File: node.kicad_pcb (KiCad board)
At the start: 2 copper layers, 46 x 38 mm, 38 parts, among them J1 USB_B_Mini, J2 TC2030_NL, J3 FFC-0.5MM-6POS, J4 Port_1, J5 Port_2, J6 FFC-0.5MM-6POS, J7 Port_3, J8 Port_4, U1 PMIC-LDO-XC6204B332MR_SOT23-5_, U2 LP2985-5.0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

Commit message: Replace 2x1 header footprint by port footprint
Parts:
- J4, J5, J7, J8: footprint Connector_PinHeader_2.54mm:PinHeader_1x02_P2.54mm_Vertical -> node:port
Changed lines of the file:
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@@
       (net 15 "Net-(D4-Pad1)"))
   )
-  (module Connector_PinHeader_2.54mm:PinHeader_1x02_P2.54mm_Vertical (layer F.Cu)
+  (module node:port (layer F.Cu)
     (at 127.254 79.629 90)
     (descr "Through hole straight pin header, 1x02, 2.54mm pitch, single row")
     (tags "Through hole pin header THT 1x02 2.54mm single row")
-    (fp_text reference J4 (at 0 -2.33 90) (layer F.SilkS) hide
+    (fp_text reference J4 (at -0.254 -1.778 90) (layer F.SilkS) hide
       (effects (font (size 1 1) (thickness 0.15)))
     )
-    (fp_text value Port_1 (at 0 4.87 90) (layer F.Fab)
+    (fp_text value Port_1 (at 0 4.318 90) (layer F.Fab)
       (effects (font (size 1 1) (thickness 0.15)))
     )
-    (fp_text user %R (at 0 1.27 180) (layer F.Fab)
-      (effects (font (size 1 1) (thickness 0.15)))
-    )
-    (fp_line (start 1.8 -1.8) (end -1.8 -1.8) (layer F.CrtYd) (width 0.05))
-    (fp_line (start 1.8 4.35) (end 1.8 -1.8) (layer F.CrtYd) (width 0.05))
-    (fp_line (start -1.8 4.35) (end 1.8 4.35) (layer F.CrtYd) (width 0.05))
-    (fp_line (start -1.8 -1.8) (end -1.8 4.35) (layer F.CrtYd) (width 0.05))
-    (fp_line (start -1.33 -1.33) (end 0 -1.33) (layer F.SilkS) (width 0.12))
-    (fp_line (start -1.33 0) (end -1.33 -1.33) (layer F.SilkS) (width 0.12))
-    (fp_line (start -1.33 1.27) (end 1.33 1.27) (layer F.SilkS) (width 0.12))
-    (fp_line (start 1.33 1.27) (end 1.33 3.87) (layer F.SilkS) (width 0.12))
-    (fp_line (start -1.33 1.27) (end -1.33 3.87) (layer F.SilkS) (width 0.12))
-    (fp_line (start -1.33 3.87) (end 1.33 3.87) (layer F.SilkS) (width 0.12))
-    (fp_line (start -1.27 -0.635) (end -0.635 -1.27) (layer F.Fab) (width 0.1))
-    (fp_line (start -1.27 3.81) (end -1.27 -0.635) (layer F.Fab) (width 0.1))
-    (fp_line (start 1.27 3.81) (end -1.27 3.81) (layer F.Fab) (width 0.1))
-    (fp_line (start 1.27 -1.27) (end 1.27 3.81) (layer F.Fab) (width 0.1))
-    (fp_line (start -0.635 -1.27) (end 1.27 -1.27) (layer F.Fab) (width 0.1))
-    (pad 2 thru_hole oval (at 0 2.54 90) (size 1.7 1.7) (drill 1) (layers *.Cu *.Mask)
-      (net 3 GND))
     (pad 1 thru_hole rect (at 0 0 90) (size 1.7 1.7) (drill 1) (layers *.Cu *.Mask)
       (net 24 "/Top Hemisphere/BNC-1"))
-    (model ${KISYS3DMOD}/Connector_PinHeader_2.54mm.3dshapes/PinHeader_1x02_P2.54mm_Vertical.wrl
-      (at (xyz 0 0 0))
-      (scale (xyz 1 1 1))
-      (rotate (xyz 0 0 0))
-    )
-  )
-  (module Connector_PinHeader_2.54mm:PinHeader_1x02_P2.54mm_Vertical (layer F.Cu)
-    (at 166.878 79.756 270)
-    (descr "Through hole straight pin header, 1x02, 2.54mm pitch, single row")
-    (tags "Through hole pin header THT 1x02 2.54mm single row")
-    (fp_text reference J5 (at 0 -2.33 270) (layer F.SilkS) hide
-      (effects (font (size 1 1) (thickness 0.15)))
-    )
-    (fp_text value Port_2 (at 0 4.87 270) (layer F.Fab)
-      (effects (font (size 1 1) (thickness 0.15)))
-    )
-    (fp_line (start -0.635 -1.27) (end 1.27 -1.27) (layer F.Fab) (width 0.1))
-    (fp_line (start 1.27 -1.27) (end 1.27 3.81) (layer F.Fab) (width 0.1))
-    (fp_line (start 1.27 3.81) (end -1.27 3.81) (layer F.Fab) (width 0.1))
-    (fp_line (start -1.27 3.81) (end -1.27 -0.635) (layer F.Fab) (width 0.1))
-    (fp_line (start -1.27 -0.635) (end -0.635 -1.27) (layer F.Fab) (width 0.1))
-    (fp_line (start -1.33 3.87) (end 1.33 3.87) (layer F.SilkS) (width 0.12))
-    (fp_line (start -1.33 1.27) (end -1.33 3.87) (layer F.SilkS) (width 0.12))
-    (fp_line (start 1.33 1.27) (end 1.33 3.87) (layer F.SilkS) (width 0.12))
-    (fp_line (start -1.33 1.27) (end 1.33 1.27) (layer F.SilkS) (width 0.12))
-    (fp_line (start -1.33 0) (end -1.33 -1.33) (layer F.SilkS) (width 0.12))
-    (fp_line (start -1.33 -1.33) (end 0 -1.33) (layer F.SilkS) (width 0.12))
-    (fp_line (start -1.8 -1.8) (end -1.8 4.35) (layer F.CrtYd) (width 0.05))
-    (fp_line (start -1.8 4.35) (end 1.8 4.35) (layer F.CrtYd) (width 0.05))
-    (fp_line (start 1.8 4.35) (end 1.8 -1.8) (layer F.CrtYd) (width 0.05))
-    (fp_line (start 1.8 -1.8) (end -1.8 -1.8) (layer F.CrtYd) (width 0.05))
-    (fp_text user %R (at 0 1.27) (layer F.Fab)
-      (effects (font (size 1 1) (thickness 0.15)))
-    )
-    (pad 1 thru_hole rect (at 0 0 270) (size 1.7 1.7) (drill 1) (layers *.Cu *.Mask)
-      (net 25 "/Top Hemisphere/BNC-2"))
-    (pad 2 thru_hole oval (at 0 2.54 270) (size 1.7 1.7) (drill 1) (layers *.Cu *.Mask)
+    (pad 2 thru_hole oval (at 0 2.54 90) (size 1.7 1.7) (drill 1) (layers *.Cu *.Mask)
       (net 3 GND))
     (model ${KISYS3DMOD}/Connector_PinHeader_2.54mm.3dshapes/PinHeader_1x02_P2.54mm_Vertical.wrl
@@
     )
   )
-  (module Connector_PinHeader_2.54mm:PinHeader_1x02_P2.54mm_Vertical (layer F.Cu)
+  (module node:port (layer F.Cu)
+    (at 166.878 79.756 270)
+    (descr "Through hole straight pin header, 1x02, 2.54mm pitch, single row")
+    (tags "Through hole pin header THT 1x02 2.54mm single row")
+    (fp_text reference J5 (at -0.254 -1.778 270) (layer F.SilkS) hide
+      (effects (font (size 1 1) (thickness 0.15)))
+    )
+    (fp_text value Port_2 (at 0 4.318 270) (layer F.Fab)
+      (effects (font (size 1 1) (thickness 0.15)))
+    )
+    (pad 2 thru_hole oval (at 0 2.54 270) (size 1.7 1.7) (drill 1) (layers *.Cu *.Mask)
+      (net 3 GND))
+    (pad 1 thru_hole rect (at 0 0 270) (size 1.7 1.7) (drill 1) (layers *.Cu *.Mask)
+      (net 25 "/Top Hemisphere/BNC-2"))
+    (model ${KISYS3DMOD}/Connector_PinHeader_2.54mm.3dshapes/PinHeader_1x02_P2.54mm_Vertical.wrl
+      (at (xyz 0 0 0))
+      (scale (xyz 1 1 1))
+      (rotate (xyz 0 0 0))
+    )
+  )
+  (module node:port (layer F.Cu)
     (at 127.127 85.487 90)
     (descr "Through hole straight pin header, 1x02, 2.54mm pitch, single row")
     (tags "Through hole pin header THT 1x02 2.54mm single row")
-    (fp_text reference J7 (at 0 -2.33 90) (layer F.SilkS) hide
+    (fp_text reference J7 (at -0.254 -1.778 90) (layer F.SilkS) hide
       (effects (font (size 1 1) (thickness 0.15)))
     )
-    (fp_text value Port_3 (at 0 4.87 90) (layer F.Fab)
+    (fp_text value Port_3 (at 0 4.318 90) (layer F.Fab)
       (effects (font (size 1 1) (thickness 0.15)))
     )
-    (fp_text user %R (at 0 1.27 180) (layer F.Fab)
-      (effects (font (size 1 1) (thickness 0.15)))
-    )
-    (fp_line (start 1.8 -1.8) (end -1.8 -1.8) (layer F.CrtYd) (width 0.05))
-    (fp_line (start 1.8 4.35) (end 1.8 -1.8) (layer F.CrtYd) (width 0.05))
-    (fp_line (start -1.8 4.35) (end 1.8 4.35) (layer F.CrtYd) (width 0.05))
-    (fp_line (start -1.8 -1.8) (end -1.8 4.35) (layer F.CrtYd) (width 0.05))
-    (fp_line (start -1.33 -1.33) (end 0 -1.33) (layer F.SilkS) (width 0.12))
-    (fp_line (start -1.33 0) (end -1.33 -1.33) (layer F.SilkS) (width 0.12))
-    (fp_line (start -1.33 1.27) (end 1.33 1.27) (layer F.SilkS) (width 0.12))
-    (fp_line (start 1.33 1.27) (end 1.33 3.87) (layer F.SilkS) (width 0.12))
-    (fp_line (start -1.33 1.27) (end -1.33 3.87) (layer F.SilkS) (width 0.12))
-    (fp_line (start -1.33 3.87) (end 1.33 3.87) (layer F.SilkS) (width 0.12))
-    (fp_line (start -1.27 -0.635) (end -0.635 -1.27) (layer F.Fab) (width 0.1))
-    (fp_line (start -1.27 3.81) (end -1.27 -0.635) (layer F.Fab) (width 0.1))
-    (fp_line (start 1.27 3.81) (end -1.27 3.81) (layer F.Fab) (width 0.1))
-    (fp_line (start 1.27 -1.27) (end 1.27 3.81) (layer F.Fab) (width 0.1))
-    (fp_line (start -0.635 -1.27) (end 1.27 -1.27) (layer F.Fab) (width 0.1))
     (pad 2 thru_hole oval (at 0 2.54 90) (size 1.7 1.7) (drill 1) (layers *.Cu *.Mask)
       (net 3 GND))
@@
     )
   )
-  (module Connector_PinHeader_2.54mm:PinHeader_1x02_P2.54mm_Vertical (layer F.Cu)
+  (module node:port (layer F.Cu)
     (at 167.005 85.233 270)
     (descr "Through hole straight pin header, 1x02, 2.54mm pitch, single row")
     (tags "Through hole pin header THT 1x02 2.54mm single row")
-    (fp_text reference J8 (at 0 -2.33 270) (layer F.SilkS) hide
+    (fp_text reference J8 (at -0.254 -1.778 270) (layer F.SilkS) hide
       (effects (font (size 1 1) (thickness 0.15)))
     )
-    (fp_text value Port_4 (at 0 4.87 270) (layer F.Fab)
-      (effects (font (size 1 1) (thickness 0.15)))
-    )
-    (fp_line (start -0.635 -1.27) (end 1.27 -1.27) (layer F.Fab) (width 0.1))
-    (fp_line (start 1.27 -1.27) (end 1.27 3.81) (layer F.Fab) (width 0.1))
-    (fp_line (start 1.27 3.81) (end -1.27 3.81) (layer F.Fab) (width 0.1))
-    (fp_line (start -1.27 3.81) (end -1.27 -0.635) (layer F.Fab) (width 0.1))
-    (fp_line (start -1.27 -0.635) (end -0.635 -1.27) (layer F.Fab) (width 0.1))
-    (fp_line (start -1.33 3.87) (end 1.33 3.87) (layer F.SilkS) (width 0.12))
-    (fp_line (start -1.33 1.27) (end -1.33 3.87) (layer F.SilkS) (width 0.12))
-    (fp_line (start 1.33 1.27) (end 1.33 3.87) (layer F.SilkS) (width 0.12))
-    (fp_line (start -1.33 1.27) (end 1.33 1.27) (layer F.SilkS) (width 0.12))
-    (fp_line (start -1.33 0) (end -1.33 -1.33) (layer F.SilkS) (width 0.12))
-    (fp_line (start -1.33 -1.33) (end 0 -1.33) (layer F.SilkS) (width 0.12))
-    (fp_line (start -1.8 -1.8) (end -1.8 4.35) (layer F.CrtYd) (width 0.05))
-    (fp_line (start -1.8 4.35) (end 1.8 4.35) (layer F.CrtYd) (width 0.05))
-    (fp_line (start 1.8 4.35) (end 1.8 -1.8) (layer F.CrtYd) (width 0.05))
-    (fp_line (start 1.8 -1.8) (end -1.8 -1.8) (layer F.CrtYd) (width 0.05))
-    (fp_text user %R (at 0 1.27) (layer F.Fab)
+    (fp_text value Port_4 (at 0 4.318 270) (layer F.Fab)
       (effects (font (size 1 1) (thickness 0.15)))
     )
@@
     (pad 2 thru_hole oval (at 0 2.54 270) (size 1.7 1.7) (drill 1) (layers *.Cu *.Mask)
       (net 3 GND))
+    (model ${KISYS3DMOD}/Connector_PinHeader_2.54mm.3dshapes/PinHeader_1x02_P2.54mm_Vertical.wrl
+      (at (xyz 0 0 0))
+      (scale (xyz 1 1 1))
+      (rotate (xyz 0 0 0))
+    )
   )
   (gr_text ⏚ (at 132.08 79.629 90) (layer B.SilkS)

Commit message: Switch to WS2812D-F5 footprints
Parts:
- D2, D3, D4, D5: footprint Connector_PinHeader_2.54mm:PinHeader_1x04_P2.54mm_Vertical -> node:WS2812D-F5

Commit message: Remove via in the middle to PTH
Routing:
- net /Top Hemisphere/DOUT-BOT: vias 1 -> 0
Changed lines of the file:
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@@
     (thickness 1)
     (drawings 119)
-    (tracks 482)
+    (tracks 481)
     (zones 0)
     (modules 38)
@@
   (segment (start 135.847 74.888) (end 135.847 72.172963) (width 0.1524) (layer F.Cu) (net 13) (status 30))
   (segment (start 152.842 78.571) (end 152.759928 78.571) (width 0.1524) (layer F.Cu) (net 14))
-  (via (at 164.78 75.904) (size 0.5) (drill 0.3) (layers F.Cu B.Cu) (net 14))
   (segment (start 164.09244 76.59156) (end 164.78 75.904) (width 0.1524) (layer F.Cu) (net 14))
   (segment (start 160.655399 80.028601) (end 164.09244 76.59156) (width 0.1524) (layer F.Cu) (net 14))

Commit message: Fix DRC errors
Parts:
- moved C10 1.83 mm to (147.1, 79.2)
- moved C5 1.83 mm to (146.1, 79.2)
- moved J3 0.40 mm to (152.4, 81.1)
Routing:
- net +5V: track 94.6 -> 97.2 mm, vias 9 -> 8
- net /Top Hemisphere/BNC-3: track 15.7 -> 13.3 mm
- net GND: track 60.7 -> 58.6 mm, vias 13 -> 11
- net /Top Hemisphere/Z-ACCEL: track 9.80 -> 11.7 mm
- net /Top Hemisphere/~RST: track 32.0 -> 30.7 mm
- net +3V3: track 24.3 -> 24.9 mm
- net /Top Hemisphere/BATT-BOT: track 20.5 -> 21.1 mm

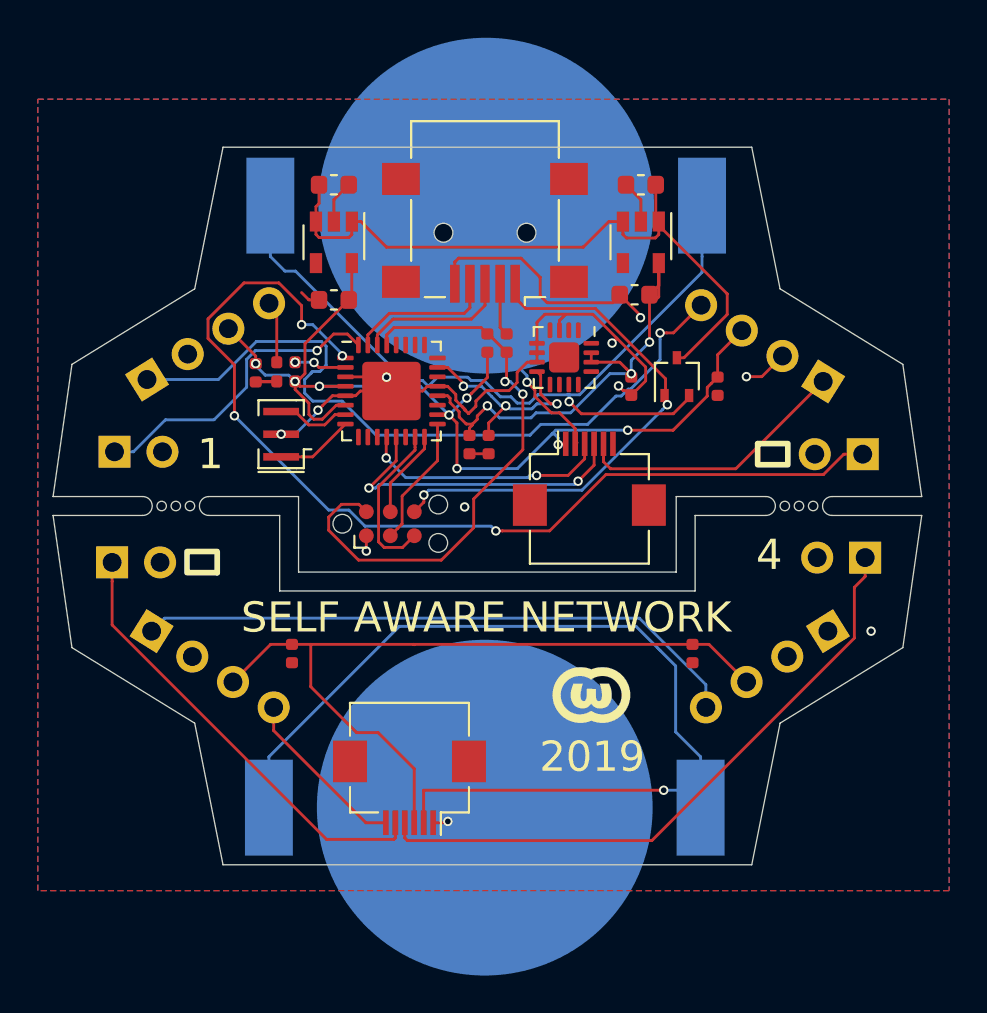
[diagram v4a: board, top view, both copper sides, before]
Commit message: Give more space to LEDs in enclosure (new outline)
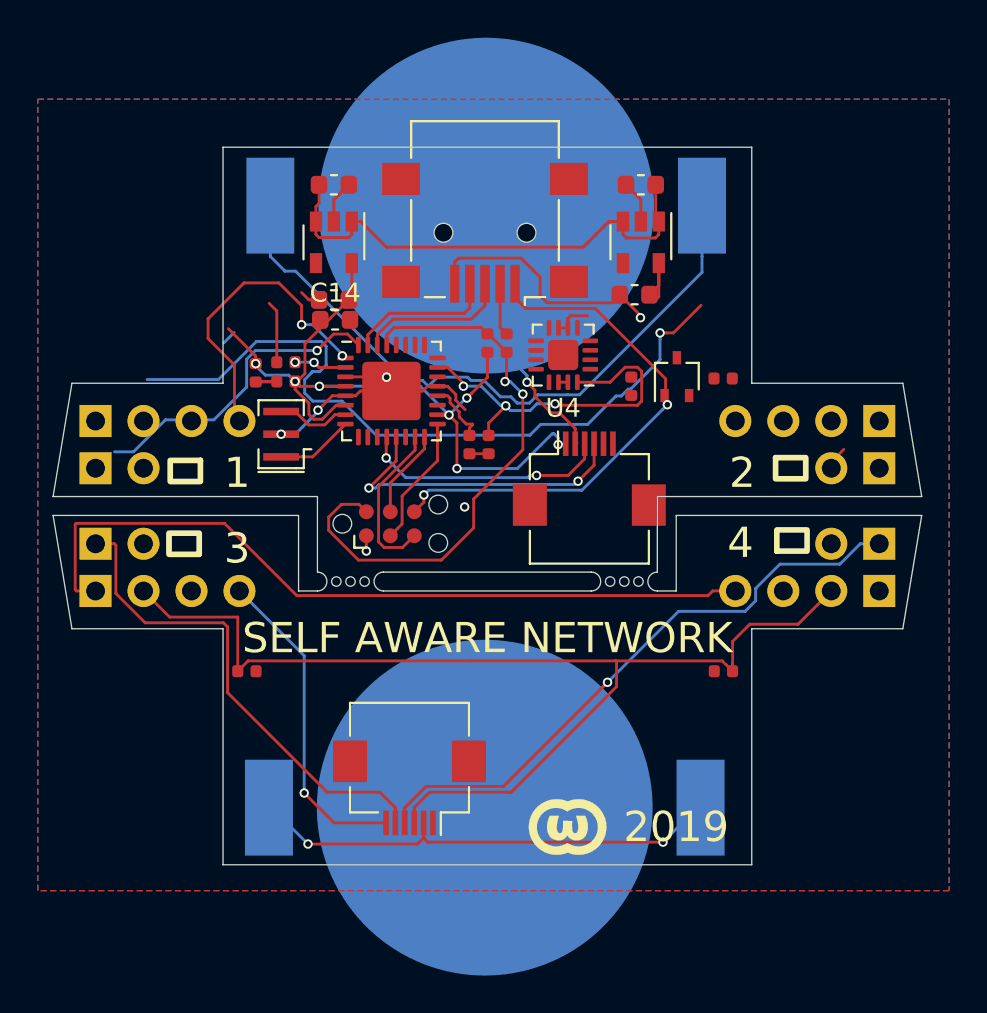
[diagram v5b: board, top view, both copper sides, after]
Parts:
- added C14: 1u, Capacitor_SMD:C_0603_1608Metric, F.Cu at (138.9, 72.6)
- D2: value LED 1 -> WS2812D-F5
- D3: value LED 2 -> WS2812D-F5
- D4: value LED 3 -> WS2812D-F5
- D5: value LED 4 -> WS2812D-F5
- U4: value ADXL335 -> ADXL337
- moved mouse-bite 10.1 mm to (154.2, 86.5)
- moved mouse-bite 10.1 mm to (139.8, 86.5)
- moved G*** 7.10 mm to (151.2, 99.5)
- moved D4 3.65 mm to (126.2, 87.0), turned to 90 degrees
- moved D3 3.64 mm to (167.8, 78.0), turned to 270 degrees
- moved D2 3.50 mm to (126.2, 78.0), turned to 90 degrees
- moved D5 3.45 mm to (167.8, 87.0), turned to 270 degrees
- moved C12 2.56 mm to (134.3, 91.2), turned to 0 degrees
- moved C13 1.89 mm to (159.5, 91.2), turned to 180 degrees
- moved J4 1.33 mm to (126.2, 80.5)
- moved J7 1.32 mm to (126.2, 84.5)
- moved J5 1.15 mm to (167.8, 80.5)
- moved J8 1.05 mm to (167.8, 84.5)
- moved C11 0.50 mm to (159.5, 75.8), turned to 180 degrees
- moved U4 0.13 mm to (151.0, 74.5), turned to 180 degrees
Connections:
- C3 pad 1: +5V -> GND
- C3 pad 2: GND -> +5V
- D2 pad 2: GND -> +5V
- D2 pad 3: +5V -> GND
- D3 pad 2: GND -> +5V
- D3 pad 3: +5V -> GND
- D4 pad 2: GND -> +5V
- D4 pad 3: +5V -> GND
- D5 pad 2: GND -> +5V
- D5 pad 3: +5V -> GND
- U4 pad 10: Net-(U4-Pad10) -> (no net)
- U4 pad 12: Net-(U4-Pad12) -> (no net)
- U4 pad 16: (no net) -> /Top Hemisphere/Z-ACCEL
- U4 pad 2: Net-(U4-Pad2) -> GND
- U4 pad 3: GND -> (no net)
- U4 pad 4: (no net) -> Net-(U4-Pad4)
- U4 pad 5: GND -> Net-(U4-Pad5)
- U4 pad 8: /Top Hemisphere/Z-ACCEL -> (no net)
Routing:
- net /Top Hemisphere/BNC-2: track 53.5 -> 16.0 mm, vias 4 -> 2
- net /Bottom hemisphere/BATT-BOT: track 52.8 -> 25.4 mm, vias 1 -> 2
- net GND: track 58.6 -> 39.2 mm, vias 11 -> 6
- net +3V3: track 24.9 -> 7.84 mm, vias 3 -> 0
- net /Top Hemisphere/DOUT-BOT: track 14.7 -> 0.00 mm
- net /Top Hemisphere/VIN: track 36.4 -> 26.3 mm
- net Net-(D4-Pad1): track 32.3 -> 41.2 mm
- net /Bottom hemisphere/DIN-BOT: track 9.19 -> 17.1 mm, vias 0 -> 1
- net /Top Hemisphere/Z-ACCEL: track 11.7 -> 19.5 mm
- net /Top Hemisphere/BATT: track 43.1 -> 35.6 mm, vias 1 -> 0
- net +5V: track 97.2 -> 102.3 mm, vias 8 -> 7
- net /Bottom hemisphere/BNC-3: track 23.8 -> 26.0 mm
- net /Bottom hemisphere/BNC-4: track 33.6 -> 32.1 mm, vias 0 -> 1
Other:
- outline, holes or cut-outs redrawn

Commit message: Reroute
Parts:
- moved C10 10.4 mm to (157.2, 76.8), turned to 0 degrees
- moved D1 7.25 mm to (159.1, 68.7)
- moved U4 4.60 mm to (155.6, 74.1)
- moved C6 1.89 mm to (138.0, 76.8), turned to 270 degrees
- moved R2 1.42 mm to (137.7, 75.2)
- moved C5 1.36 mm to (146.2, 77.9)
- moved C3 1.09 mm to (138.9, 70.5)
- moved J3 1.05 mm to (151.3, 81.0)
- moved C4 0.96 mm to (155.1, 70.4)
- moved U1 0.94 mm to (155.1, 67.6)
- moved C11 0.92 mm to (160.3, 75.3), turned to 90 degrees
- moved C8 0.88 mm to (155.2, 76.8), turned to 180 degrees
- moved U2 0.84 mm to (138.9, 67.7)
- moved Y1 0.71 mm to (136.2, 79.4)
- moved C9 0.71 mm to (134.2, 75.9), turned to 90 degrees
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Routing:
- net +5V: track 102.3 -> 148.2 mm, vias 7 -> 2
- net GND: track 39.2 -> 11.4 mm, vias 6 -> 19
- net /Top Hemisphere/BNC-2: track 16.0 -> 41.3 mm, vias 2 -> 1
- net +3V3: track 7.84 -> 26.4 mm, vias 0 -> 2
- net /Top Hemisphere/DOUT-BOT: track 0.00 -> 17.8 mm, vias 0 -> 1
- net /Top Hemisphere/~RST: track 30.7 -> 21.5 mm
- net Net-(D2-Pad1): track 39.3 -> 48.0 mm, vias 1 -> 0
- net /Top Hemisphere/BATT: track 35.6 -> 29.7 mm, vias 0 -> 2
- net /Top Hemisphere/Z-ACCEL: track 19.5 -> 25.0 mm, vias 3 -> 0
- net /Top Hemisphere/VIN: track 26.3 -> 31.1 mm
- net /Top Hemisphere/BNC-4: track 16.9 -> 13.7 mm
- net /Top Hemisphere/BNC-1: track 16.6 -> 18.3 mm
- net /Top Hemisphere/BNC-3: track 13.3 -> 11.7 mm
- net Net-(R2-Pad2): track 2.78 -> 1.34 mm, vias 2 -> 0
- net /Top Hemisphere/DIN-TOP: track 3.29 -> 4.49 mm, vias 0 -> 1
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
